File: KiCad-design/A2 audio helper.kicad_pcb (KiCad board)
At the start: 2 copper layers, 45 x 83.5 mm, 37 parts, among them J1 PIN HEADER 1x2, J10 PIN HEADER 1x2, J11 PIN HEADER 1x3, J12 PIN HEADER 1x3, J13 PIN HEADER 2x4, J15 PIN HEADER 2x6, J16 PIN HEADER 2x6, J17 SJ1-3515N, J3 PIN HEADER 1x2, J4 SJ1-3515N, J5 PIN HEADER 1x3, J6 PIN HEADER 1x3, J7 SJ1-3515N, J9 PIN HEADER 1x2, K1 SR11-5V-200-2C, SW2 SW_DPDT_x2, U1 pam8403

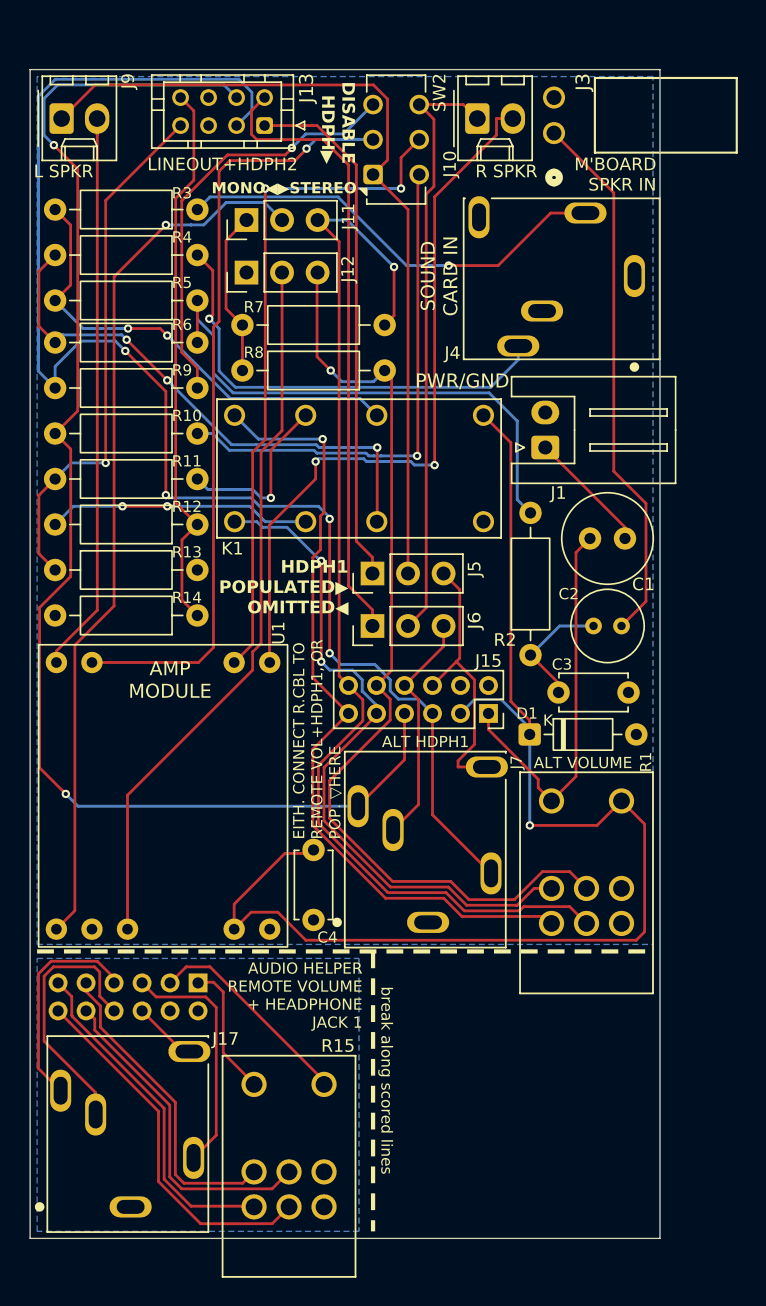
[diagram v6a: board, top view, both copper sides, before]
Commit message: trim some footprints to edges, pos'n consistently
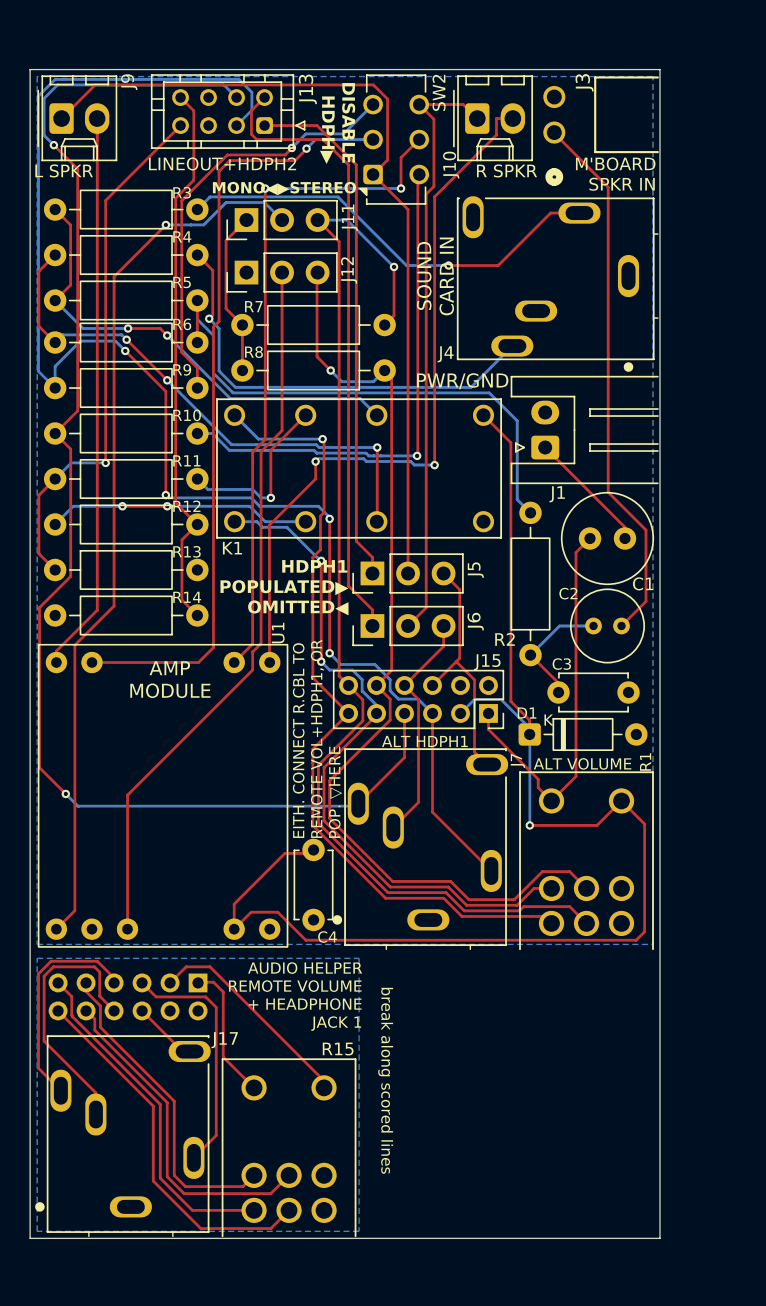
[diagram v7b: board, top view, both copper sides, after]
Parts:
- moved J4 0.42 mm to (92.8, 50.8)
- moved R15 0.25 mm to (68.5, 115.0)
- moved J7 0.18 mm to (78.5, 96.8)
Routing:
- net HP1_TN: track 19.9 -> 17.5 mm
- net /JACK_R: track 32.8 -> 31.8 mm

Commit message: change 3d model for vol knob
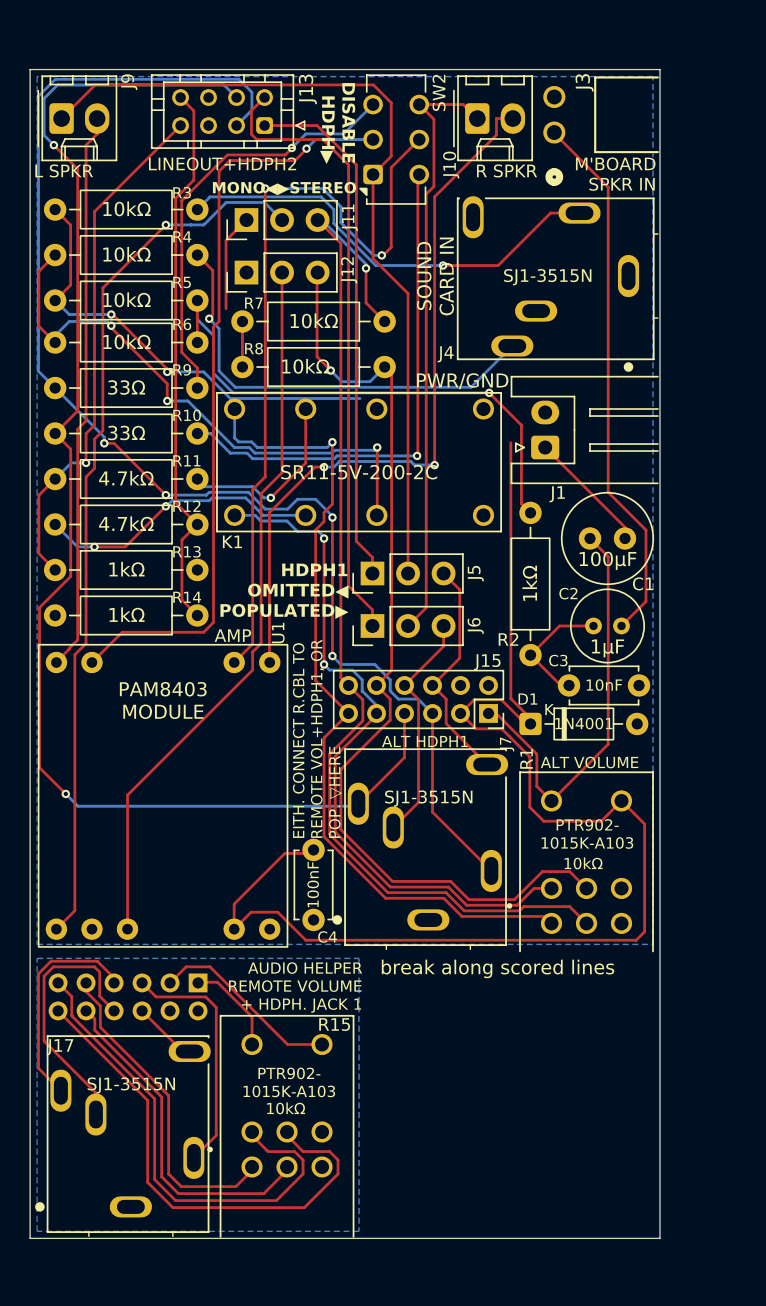
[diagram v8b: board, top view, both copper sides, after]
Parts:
- R1, R15: footprint PTR902-1020K-A502:TRIM_PTR902-1020K-A502 -> PTN09S2_H10215K1A:TRIM_PTN09S2-H10215K1A
- moved R1 7.50 mm to (89.8, 102.0), turned to 0 degrees
- moved R15 4.40 mm to (68.4, 119.4), turned to 0 degrees
- moved C3 0.90 mm to (88.5, 80.0)
- moved D1 0.75 mm to (85.8, 82.8)
- moved K1 0.45 mm to (73.5, 64.0)
- moved R7 0.25 mm to (75.3, 54.0)
- moved R8 0.25 mm to (75.3, 57.2)
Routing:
- net /Daughterboard/RMT_SRC_L: track 24.7 -> 34.3 mm
- net /Daughterboard/REM_VOL_L: track 26.6 -> 35.6 mm
- net HP1_T: track 104.4 -> 97.5 mm
- net Net-(SW2B-B): track 48.5 -> 55.2 mm
- net /Daughterboard/RMT_V_IN: track 9.95 -> 6.91 mm
- net VOL_L: track 79.4 -> 76.9 mm
- net /INPUT_AUDIO_R: track 39.1 -> 41.4 mm
- net /Daughterboard/RMT_V_AMP: track 15.4 -> 13.6 mm
- net /LINEOUT_SOURCE_R: track 18.9 -> 20.6 mm
- net /MONO_MIX: track 11.9 -> 10.2 mm
- net SRC_L: track 57.0 -> 58.7 mm
- net /INPUT_AUDIO_L: track 33.8 -> 32.2 mm
- net V_AMP: track 95.5 -> 94.1 mm, vias 1 -> 0
- net V_IN: track 28.1 -> 29.5 mm
- net Net-(SW2A-B): track 55.3 -> 54.2 mm
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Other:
- board text added: "AMP"
- board text added: "AUDIO HELPER REMOTE VOLUME + HDPH. JACK 1"
- board text added: "HDPH1 OMITTED◀ POPULATED▶ ︎"
- board text added: "PAM8403 MODULE"
- board text added: "PTR902- 1015K-A103"
- board text removed: "AMP MODULE"
- board text removed: "AUDIO HELPER REMOTE VOLUME + HEADPHONE JACK 1"
- board text removed: "HDPH1 POPULATED▶ ︎OMITTED◀"
